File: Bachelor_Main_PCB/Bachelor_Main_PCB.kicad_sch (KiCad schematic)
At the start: 4 parts

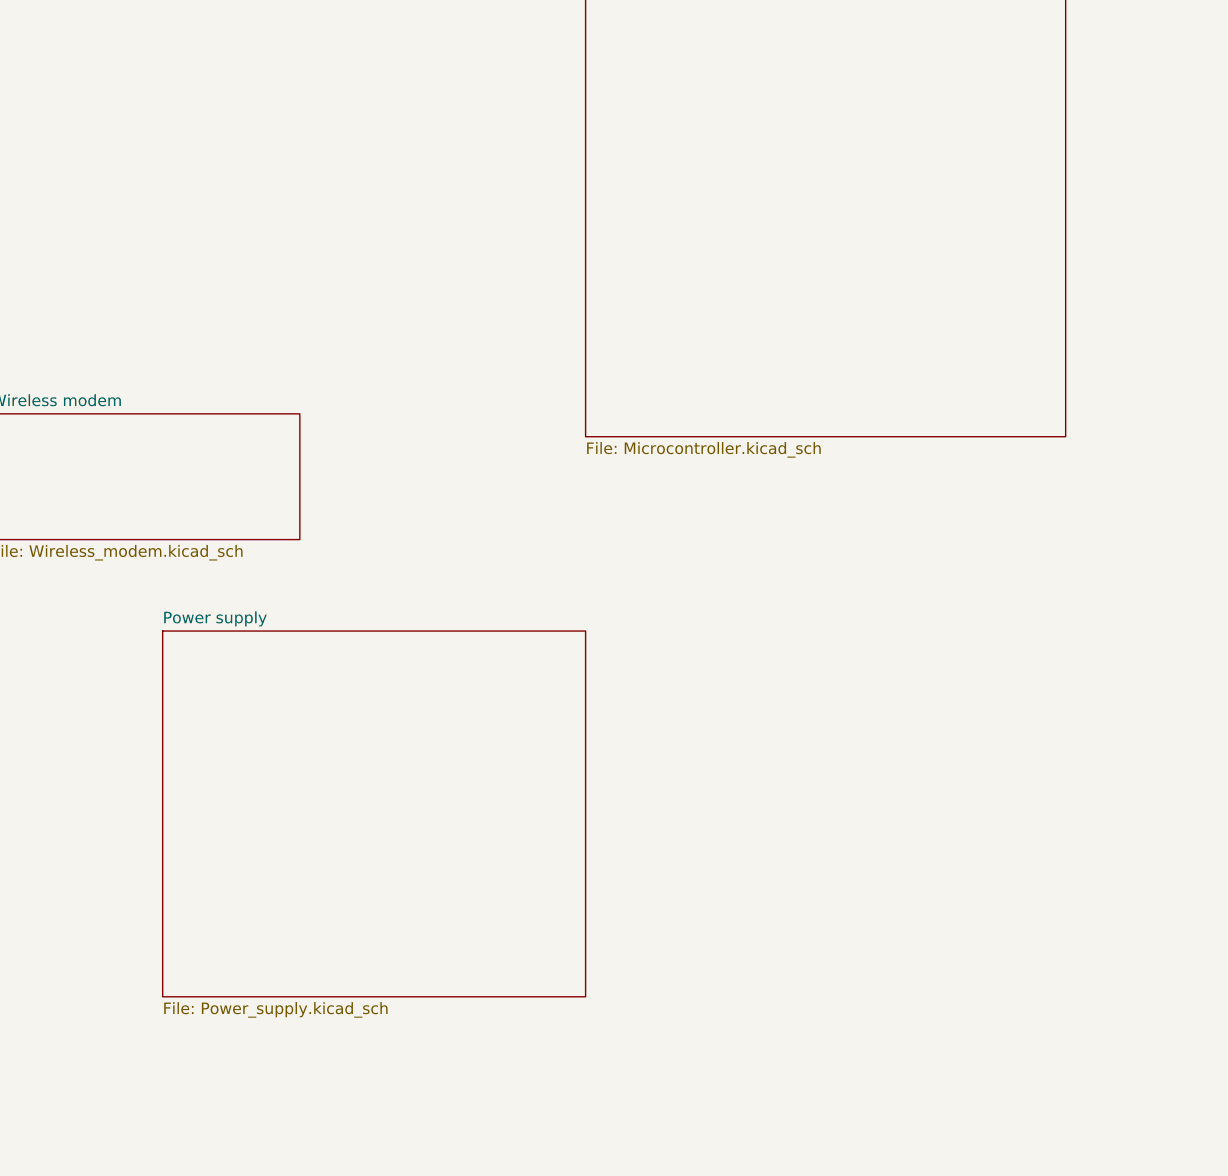
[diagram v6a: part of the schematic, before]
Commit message: Route RPI USB
PS: we need a USB hub
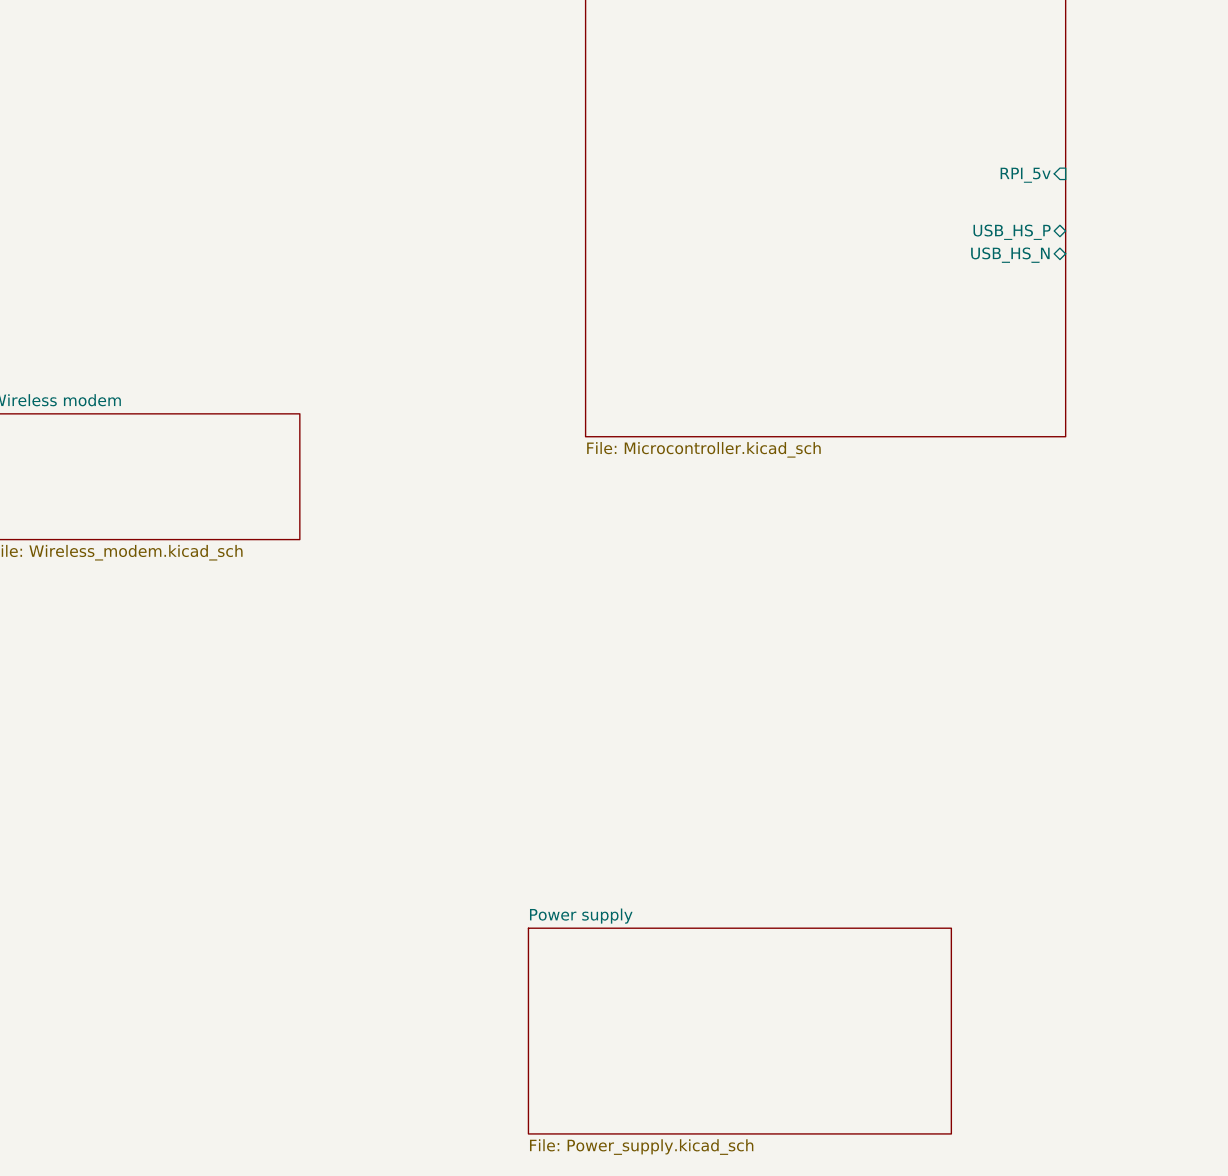
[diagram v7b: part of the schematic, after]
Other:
- sheet Microcontroller ports: added RPI_5v, USB_HS_N, USB_HS_P; removed none
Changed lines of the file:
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@@
 	)
 	(sheet
-		(at 64.77 127)
-		(size 46.99 40.64)
+		(at 105.41 160.02)
+		(size 46.99 22.86)
 		(exclude_from_sim no)
 		(in_bom yes)
@@
 		)
 		(property "Sheetname" "Power supply"
-			(at 64.77 126.2884 0)
+			(at 105.41 159.3084 0)
 			(effects
 				(font
@@
 		)
 		(property "Sheetfile" "Power_supply.kicad_sch"
-			(at 64.77 168.2246 0)
+			(at 105.41 183.4646 0)
 			(effects
 				(font
@@
 			)
 		)
+		(pin "RPI_5v" input
+			(at 165.1 76.2 0)
+			(effects
+				(font
+					(size 1.27 1.27)
+				)
+				(justify right)
+			)
+		)
+		(pin "USB_HS_N" bidirectional
+			(at 165.1 85.09 0)
+			(effects
+				(font
+					(size 1.27 1.27)
+				)
+				(justify right)
+			)
+		)
+		(pin "USB_HS_P" bidirectional
+			(at 165.1 82.55 0)
+			(effects
+				(font
+					(size 1.27 1.27)
+				)
+				(justify right)
+			)
+		)

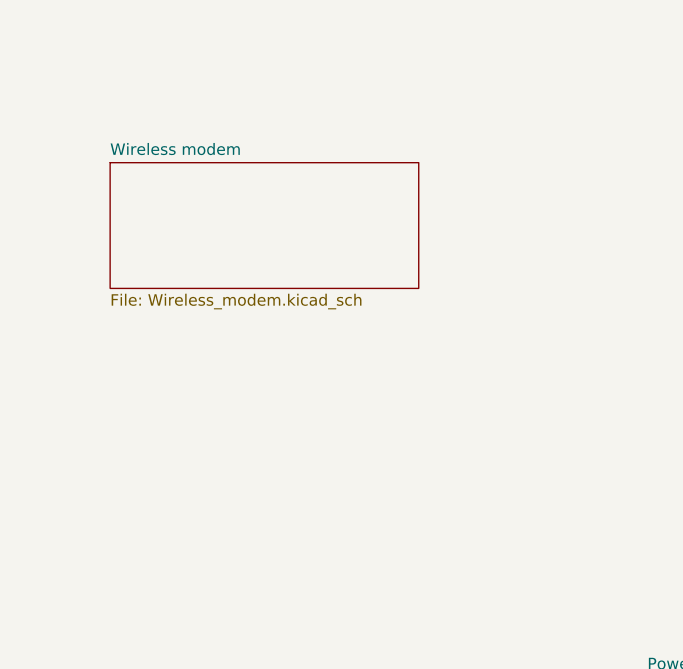
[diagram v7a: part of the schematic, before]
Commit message: Route all MODEM to RPI pins (except USB HS)
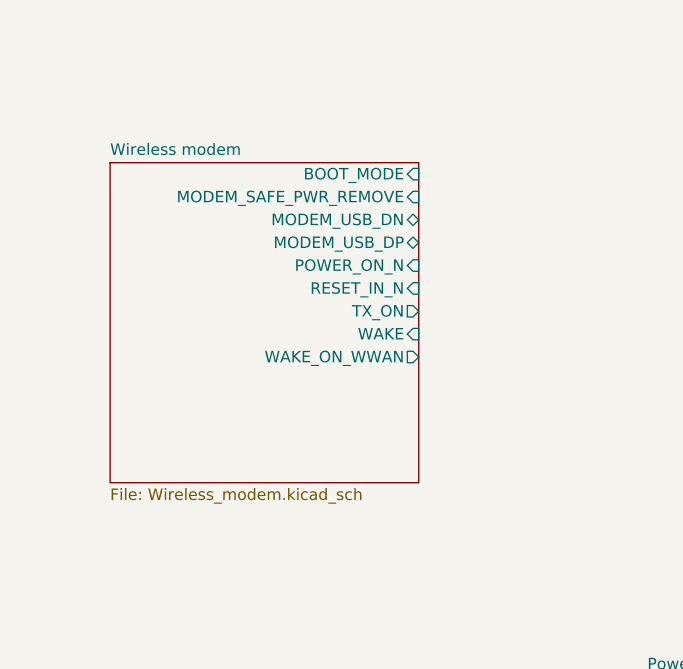
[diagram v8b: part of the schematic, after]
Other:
- sheet Wireless modem ports: added BOOT_MODE, MODEM_SAFE_PWR_REMOVE, MODEM_USB_DN, MODEM_USB_DP, POWER_ON_N, RESET_IN_N, TX_ON, WAKE, WAKE_ON_WWAN; removed none
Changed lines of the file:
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@@
 	(sheet
 		(at 45.72 102.87)
-		(size 34.29 13.97)
+		(size 34.29 35.56)
 		(exclude_from_sim no)
 		(in_bom yes)
@@
 		)
 		(property "Sheetfile" "Wireless_modem.kicad_sch"
-			(at 45.72 117.4246 0)
+			(at 45.72 139.0146 0)
 			(effects
 				(font
@@
 			)
 		)
+		(pin "BOOT_MODE" input
+			(at 80.01 104.14 0)
+			(effects
+				(font
+					(size 1.27 1.27)
+				)
+				(justify right)
+			)
+		)
+		(pin "MODEM_SAFE_PWR_REMOVE" input
+			(at 80.01 106.68 0)
+			(effects
+				(font
+					(size 1.27 1.27)
+				)
+				(justify right)
+			)
+		)
+		(pin "MODEM_USB_DN" bidirectional
+			(at 80.01 109.22 0)
+			(effects
+				(font
+					(size 1.27 1.27)
+				)
+				(justify right)
+			)
+		)
+		(pin "MODEM_USB_DP" bidirectional
+			(at 80.01 111.76 0)
+			(effects
+				(font
+					(size 1.27 1.27)
+				)
+				(justify right)
+			)
+		)
+		(pin "POWER_ON_N" input
+			(at 80.01 114.3 0)
+			(effects
+				(font
+					(size 1.27 1.27)
+				)
+				(justify right)
+			)
+		)
+		(pin "RESET_IN_N" input
+			(at 80.01 116.84 0)
+			(effects
+				(font
+					(size 1.27 1.27)
+				)
+				(justify right)
+			)
+		)
+		(pin "TX_ON" output
+			(at 80.01 119.38 0)
+			(effects
+				(font
+					(size 1.27 1.27)
+				)
+				(justify right)
+			)
+		)
+		(pin "WAKE" input
+			(at 80.01 121.92 0)
+			(effects
+				(font
+					(size 1.27 1.27)
+				)
+				(justify right)
+			)
+		)
+		(pin "WAKE_ON_WWAN" output
+			(at 80.01 124.46 0)
+			(effects
+				(font
+					(size 1.27 1.27)
+				)
+				(justify right)
+			)
+		)
